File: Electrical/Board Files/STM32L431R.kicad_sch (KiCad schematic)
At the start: 11 parts

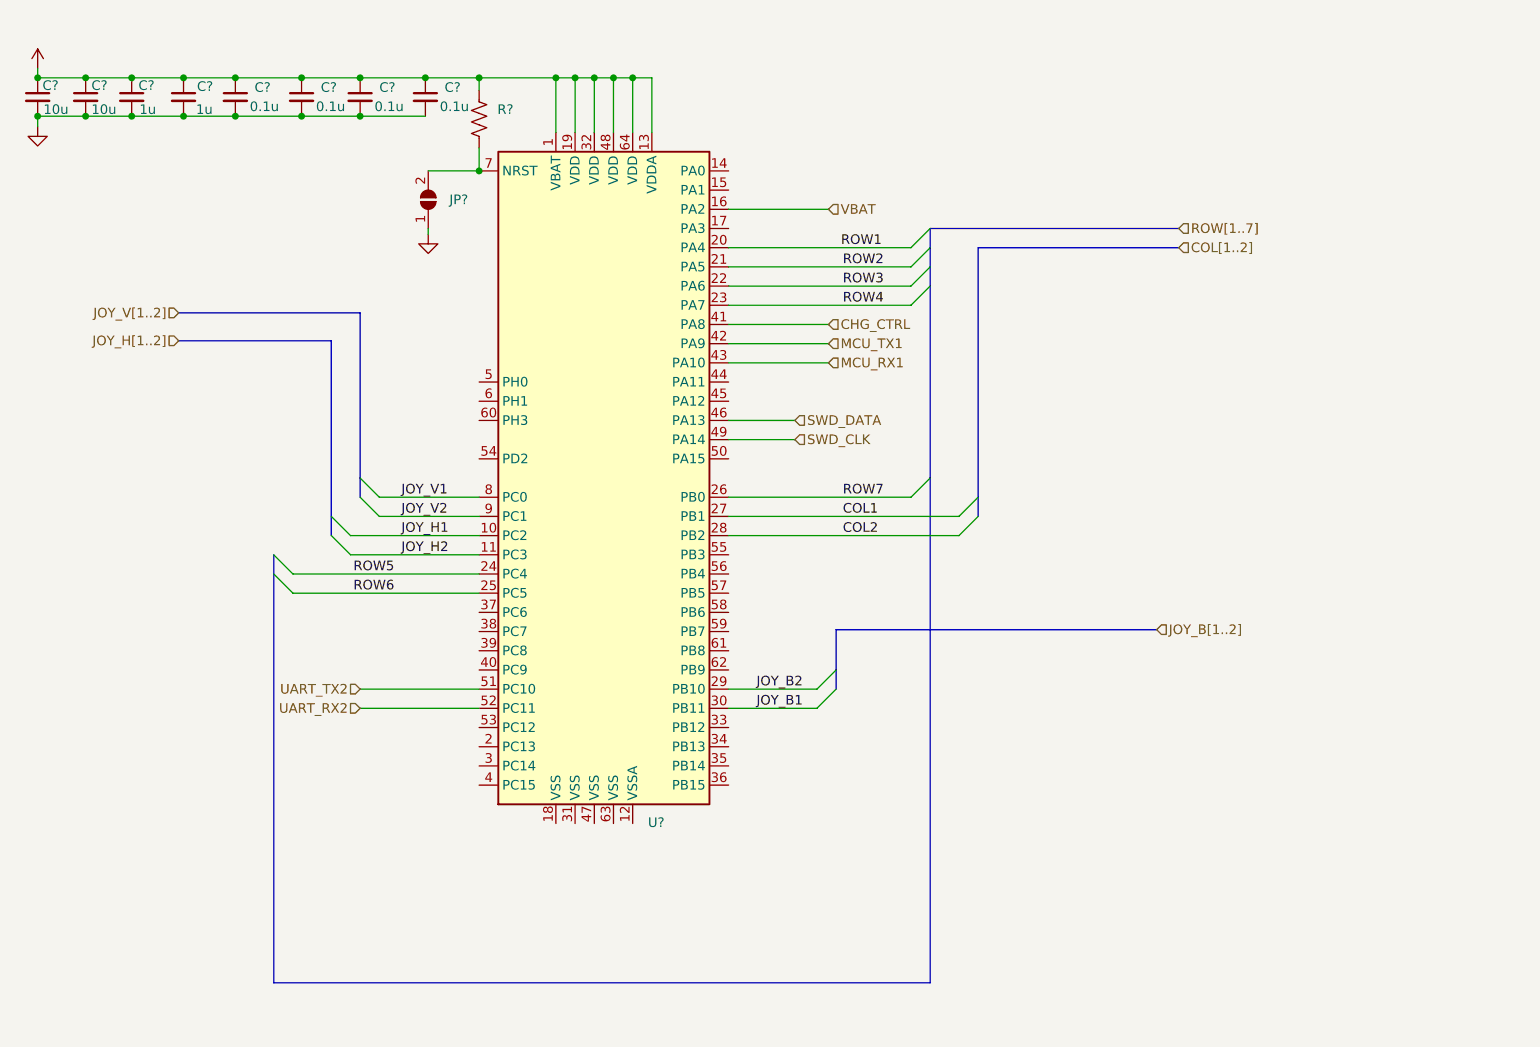
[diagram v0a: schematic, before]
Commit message: Adding new block diagram
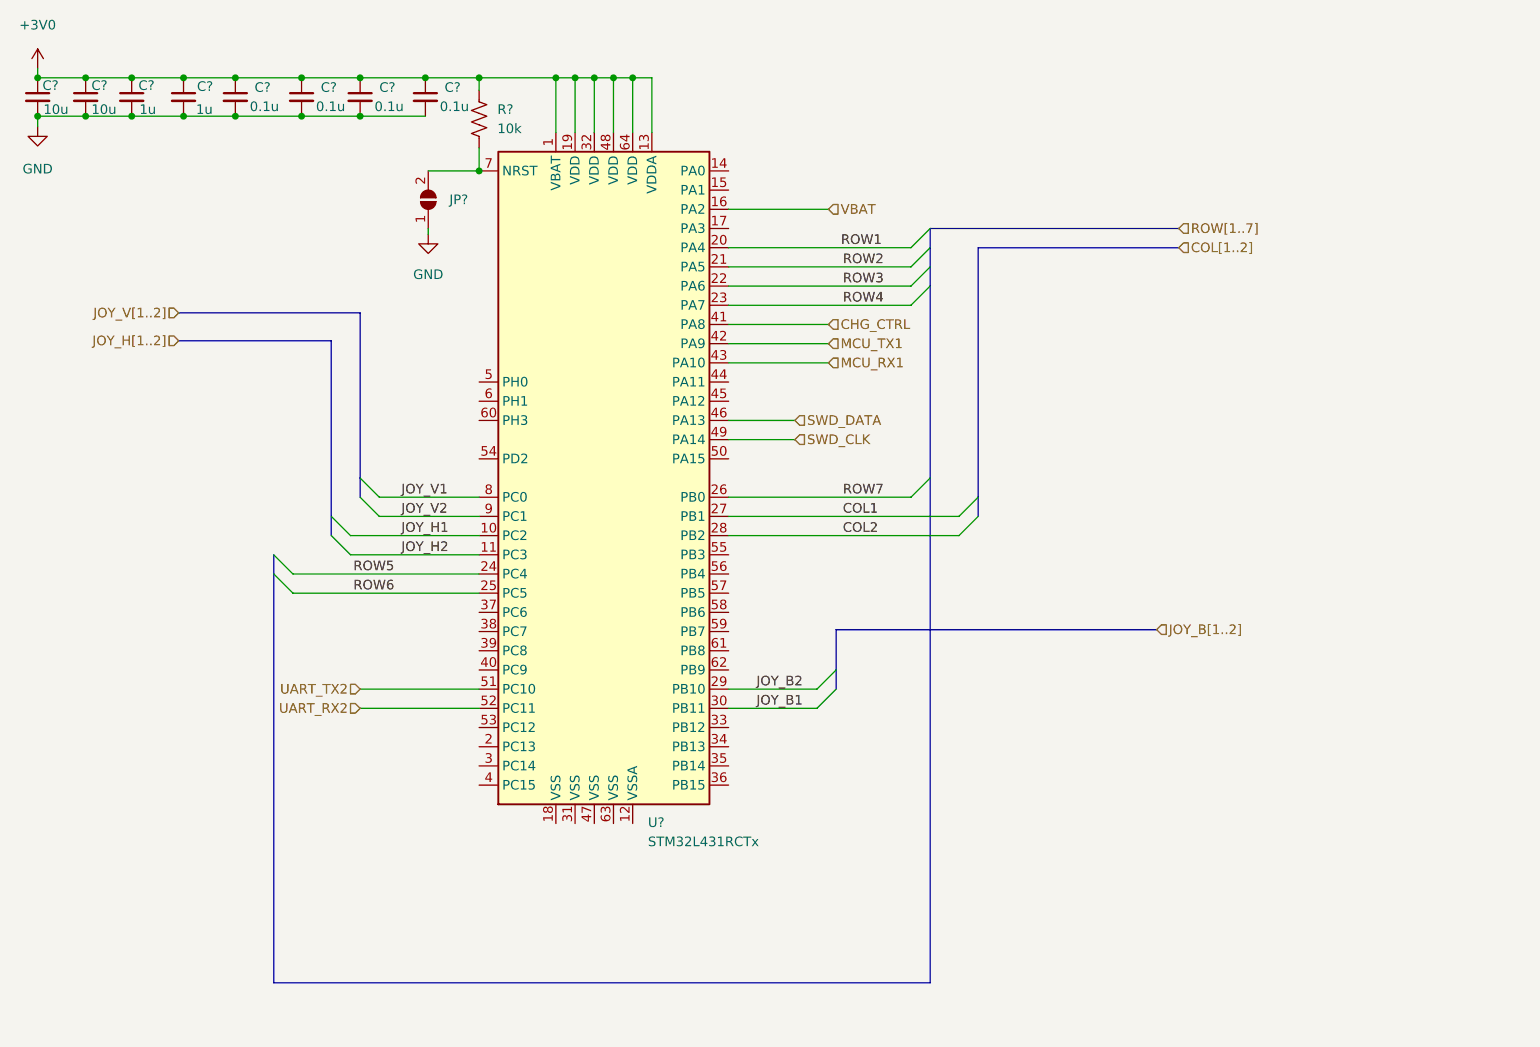
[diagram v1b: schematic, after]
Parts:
- JP?: value (none) -> SolderJumper_2_Open
- R?: value (none) -> 10k
- U?: value (none) -> STM32L431RCTx; footprint (none) -> Package_QFP:LQFP-64_10x10mm_P0.5mm
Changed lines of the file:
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@@
       (effects (font (size 1.27 1.27)) (justify left))
     )
-    (property "Value" "" (id 1) (at 107.95 39.1159 0)
+    (property "Value" "10k" (id 1) (at 107.95 39.1159 0)
       (effects (font (size 1.27 1.27)) (justify left))
     )
@@
       (effects (font (size 1.27 1.27)) hide)
     )
-    (property "Value" "" (id 1) (at 98.806 58.42 0))
+    (property "Value" "GND" (id 1) (at 98.806 58.42 0))
     (property "Footprint" "" (id 2) (at 98.806 53.086 0)
       (effects (font (size 1.27 1.27)) hide)
@@
       (effects (font (size 1.27 1.27)) hide)
     )
-    (property "Value" "" (id 1) (at 47.117 44.45 0))
+    (property "Value" "GND" (id 1) (at 47.117 44.45 0))
     (property "Footprint" "" (id 2) (at 47.117 38.862 0)
       (effects (font (size 1.27 1.27)) hide)
@@
       (effects (font (size 1.27 1.27)) hide)
     )
-    (property "Value" "" (id 1) (at 47.117 25.4 0))
+    (property "Value" "+3V0" (id 1) (at 47.117 25.4 0))
     (property "Footprint" "" (id 2) (at 47.117 31.115 0)
       (effects (font (size 1.27 1.27)) hide)
@@
       (effects (font (size 1.27 1.27)) (justify right))
     )
-    (property "Value" "" (id 1) (at 101.6 49.7839 90)
+    (property "Value" "SolderJumper_2_Open" (id 1) (at 101.6 49.7839 90)
       (effects (font (size 1.27 1.27)) (justify right) hide)
     )
@@
       (effects (font (size 1.27 1.27)) (justify left))
     )
-    (property "Value" "" (id 1) (at 127.8764 133.477 0)
-      (effects (font (size 1.27 1.27)) (justify left))
-    )
-    (property "Footprint" "" (id 2) (at 108.077 128.524 0)
+    (property "Value" "STM32L431RCTx" (id 1) (at 127.8764 133.477 0)
+      (effects (font (size 1.27 1.27)) (justify left))
+    )
+    (property "Footprint" "Package_QFP:LQFP-64_10x10mm_P0.5mm" (id 2) (at 108.077 128.524 0)
       (effects (font (size 1.27 1.27)) (justify right) hide)
     )

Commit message: Updating Files
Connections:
- net GND: now also U?.12 (VSSA), U?.18 (VSS), U?.31 (VSS), U?.47 (VSS), U?.63 (VSS)
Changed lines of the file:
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@@
   (junction (at 98.425 32.385) (diameter 0) (color 0 0 0 0)
   )
+  (junction (at 123.317 131.064) (diameter 0) (color 0 0 0 0)
+  )
+  (junction (at 118.237 131.064) (diameter 0) (color 0 0 0 0)
+  )
   (junction (at 82.042 32.385) (diameter 0) (color 0 0 0 0)
   )
@@
   (junction (at 53.467 37.465) (diameter 0) (color 0 0 0 0)
   )
+  (junction (at 115.697 131.064) (diameter 0) (color 0 0 0 0)
+  )
   (junction (at 66.421 32.385) (diameter 0) (color 0 0 0 0)
   )
@@
   (junction (at 47.117 32.385) (diameter 0) (color 0 0 0 0)
   )
+  (junction (at 120.777 131.064) (diameter 0) (color 0 0 0 0)
+  )
   (junction (at 105.537 32.385) (diameter 0) (color 0 0 0 0)
   )
@@
     (stroke (width 0) (type default) (color 0 0 0 0))
   )
-  (wire (pts (xy 138.557 80.264) (xy 147.32 80.264))
+  (wire (pts (xy 138.557 80.264) (xy 195.834 80.264))
     (stroke (width 0) (type default) (color 0 0 0 0))
   )
@@
     (stroke (width 0) (type default) (color 0 0 0 0))
   )
+  (wire (pts (xy 115.697 131.064) (xy 110.49 131.064))
+    (stroke (width 0) (type default) (color 0 0 0 0))
+  )
   (wire (pts (xy 80.899 100.584) (xy 105.537 100.584))
     (stroke (width 0) (type default) (color 0 0 0 0))
@@
     (stroke (width 0) (type default) (color 0 0 0 0))
   )
-  (wire (pts (xy 138.557 67.564) (xy 151.765 67.564))
+  (wire (pts (xy 138.557 67.564) (xy 195.58 67.564))
     (stroke (width 0) (type default) (color 0 0 0 0))
   )
@@
     (stroke (width 0) (type default) (color 0 0 0 0))
   )
+  (wire (pts (xy 120.777 131.064) (xy 118.237 131.064))
+    (stroke (width 0) (type default) (color 0 0 0 0))
+  )
   (bus (pts (xy 89.789 85.344) (xy 89.789 87.884))
     (stroke (width 0) (type default) (color 0 0 0 0))
   )
-  (wire (pts (xy 138.557 65.024) (xy 151.765 65.024))
+  (wire (pts (xy 138.557 65.024) (xy 195.58 65.024))
     (stroke (width 0) (type default) (color 0 0 0 0))
   )
@@
     (stroke (width 0) (type default) (color 0 0 0 0))
   )
+  (wire (pts (xy 125.857 131.064) (xy 123.317 131.064))
+    (stroke (width 0) (type default) (color 0 0 0 0))
+  )
+  (wire (pts (xy 123.317 131.064) (xy 120.777 131.064))
+    (stroke (width 0) (type default) (color 0 0 0 0))
+  )
   (wire (pts (xy 105.537 32.385) (xy 115.697 32.385))
     (stroke (width 0) (type default) (color 0 0 0 0))
@@
     (stroke (width 0) (type default) (color 0 0 0 0))
   )
-  (wire (pts (xy 138.557 77.724) (xy 147.32 77.724))
+  (wire (pts (xy 138.557 77.724) (xy 195.834 77.724))
     (stroke (width 0) (type default) (color 0 0 0 0))
   )
@@
     (stroke (width 0) (type default) (color 0 0 0 0))
   )
+  (wire (pts (xy 118.237 131.064) (xy 115.697 131.064))
+    (stroke (width 0) (type default) (color 0 0 0 0))
+  )
   (wire (pts (xy 120.777 32.385) (xy 120.777 39.624))
     (stroke (width 0) (type default) (color 0 0 0 0))
@@
     (stroke (width 0) (type default) (color 0 0 0 0))
   )
+  (wire (pts (xy 110.49 131.064) (xy 110.49 132.08))
+    (stroke (width 0) (type default) (color 0 0 0 0))
+  )
   (bus (pts (xy 171.577 87.884) (xy 171.577 54.864))
     (stroke (width 0) (type default) (color 0 0 0 0))
@@
     (stroke (width 0) (type default) (color 0 0 0 0))
   )
-  (wire (pts (xy 138.557 70.104) (xy 151.765 70.104))
+  (wire (pts (xy 138.557 70.104) (xy 195.58 70.104))
     (stroke (width 0) (type default) (color 0 0 0 0))
   )
@@
     (effects (font (size 1.27 1.27)) (justify left))
   )
-  (hierarchical_label "SWD_CLK" (shape input) (at 147.32 80.264 0)
+  (hierarchical_label "SWD_CLK" (shape input) (at 195.834 80.264 0)
     (effects (font (size 1.27 1.27)) (justify left))
   )
@@
     (effects (font (size 1.27 1.27)) (justify left))
   )
-  (hierarchical_label "CHG_CTRL" (shape input) (at 151.765 65.024 0)
+  (hierarchical_label "CHG_CTRL" (shape input) (at 195.58 65.024 0)
     (effects (font (size 1.27 1.27)) (justify left))
   )
-  (hierarchical_label "MCU_RX1" (shape input) (at 151.765 70.104 0)
+  (hierarchical_label "MCU_RX1" (shape input) (at 195.58 70.104 0)
     (effects (font (size 1.27 1.27)) (justify left))
   )
-  (hierarchical_label "SWD_DATA" (shape input) (at 147.32 77.724 0)
+  (hierarchical_label "SWD_DATA" (shape input) (at 195.834 77.724 0)
     (effects (font (size 1.27 1.27)) (justify left))
   )
-  (hierarchical_label "MCU_TX1" (shape input) (at 151.765 67.564 0)
+  (hierarchical_label "MCU_TX1" (shape input) (at 195.58 67.564 0)
     (effects (font (size 1.27 1.27)) (justify left))
   )
@@
     (pin "2")
   )
+  (symbol (lib_id "power:GND") (at 110.49 132.08 0) (unit 1)
+    (in_bom yes) (on_board yes) (fields_autoplaced)
+    (property "Reference" "#PWR?" (id 0) (at 110.49 138.43 0)
+      (effects (font (size 1.27 1.27)) hide)
+    )
+    (property "Value" "GND" (id 1) (at 110.49 137.414 0))
+    (property "Footprint" "" (id 2) (at 110.49 132.08 0)
+      (effects (font (size 1.27 1.27)) hide)
+    )
+    (property "Datasheet" "" (id 3) (at 110.49 132.08 0)
+      (effects (font (size 1.27 1.27)) hide)
+    )
+    (pin "1")
+  )
   (symbol (lib_id "Device:C_Small") (at 47.117 34.925 0) (unit 1)

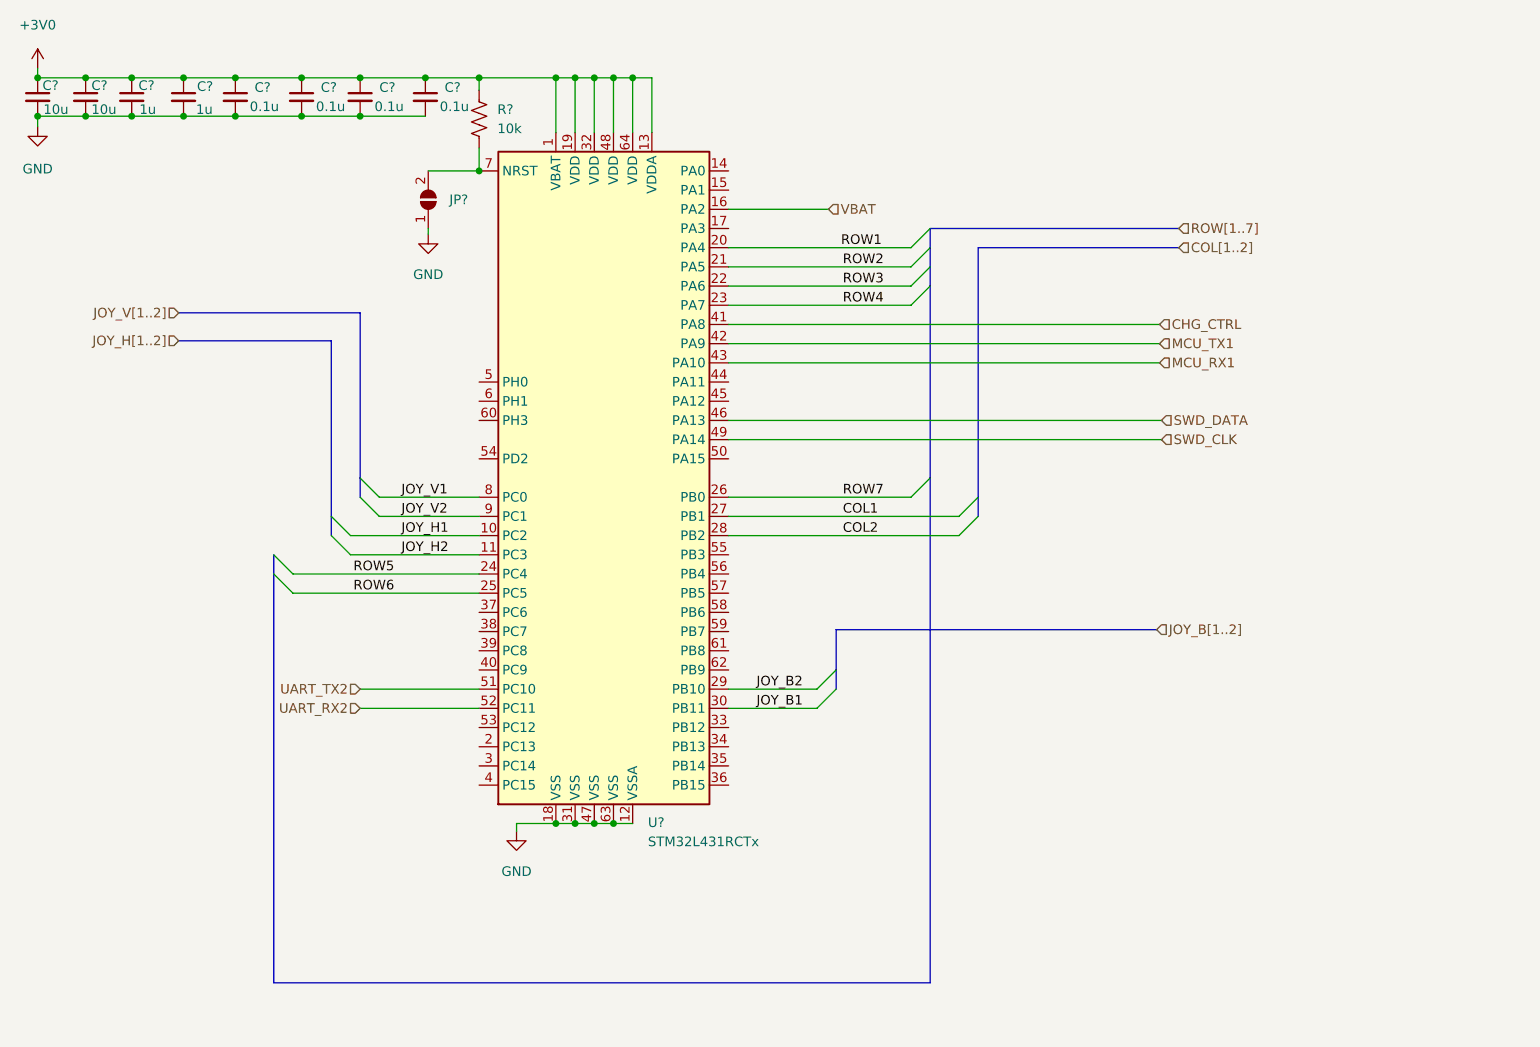
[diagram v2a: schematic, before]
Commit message: Updating for 3v3 operation
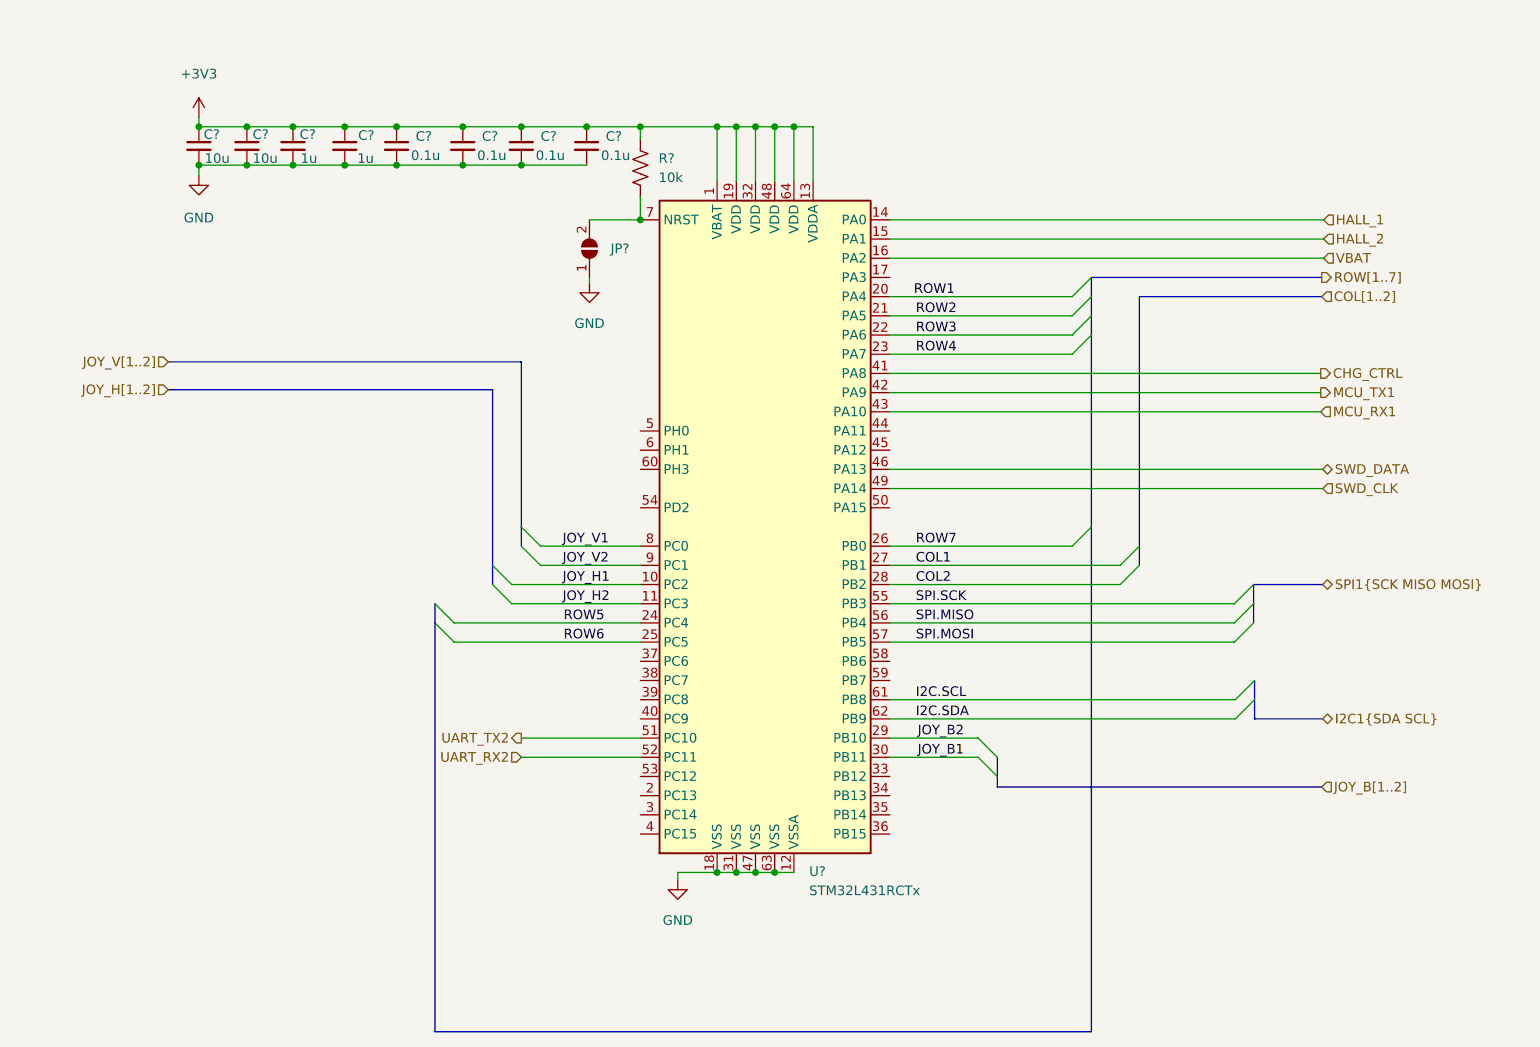
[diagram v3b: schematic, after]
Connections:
- net HALL_1: now reaches U?.14 (PA0)
- net HALL_2: now reaches U?.15 (PA1)
- net SPI.SCK: now reaches U?.55 (PB3)
- net SPI.MISO: now reaches U?.56 (PB4)
- net SPI.MOSI: now reaches U?.57 (PB5)
- net I2C.SCL: now reaches U?.61 (PB8)
- net I2C.SDA: now reaches U?.62 (PB9)
- net +3V0 renamed +3V3
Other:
- moved on the sheet: C?, JP?, R?, U?
